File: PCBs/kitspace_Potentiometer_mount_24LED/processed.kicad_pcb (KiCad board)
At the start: 2 copper layers, 143.6 x 36.5 mm, 27 parts

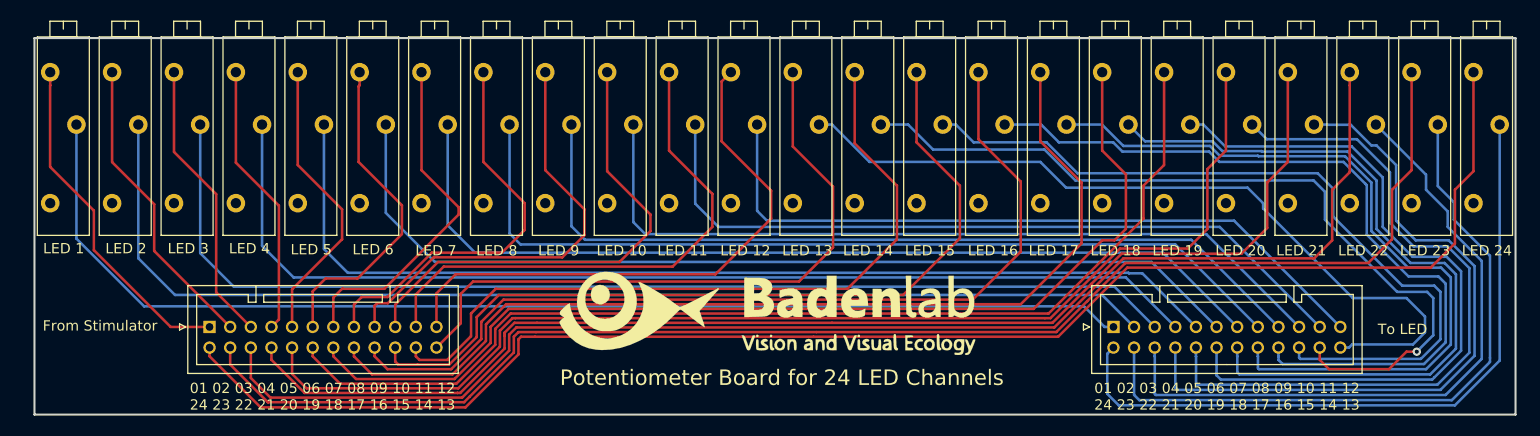
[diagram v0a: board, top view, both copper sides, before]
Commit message: recheck all circuits and clean up fill zone by rerouting the nets using freerouting and manually
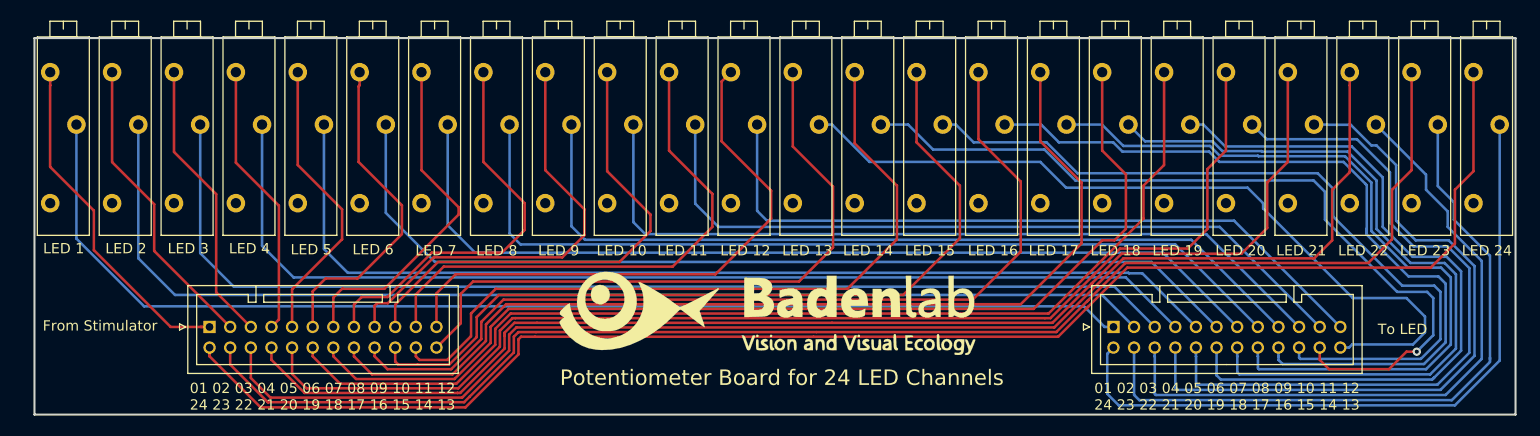
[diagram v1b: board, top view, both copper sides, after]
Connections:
-  LED 11 pad 1: (no net) -> Net-(RV11-Pad1)
- LED 1 pad 1: (no net) -> Net-(RV1-Pad1)
- LED 10 pad 1: (no net) -> Net-(RV10-Pad1)
- LED 12 pad 1: (no net) -> Net-(RV12-Pad1)
- LED 13 pad 1: (no net) -> Net-(RV13-Pad1)
- LED 14 pad 1: (no net) -> Net-(RV14-Pad1)
- LED 15 pad 1: (no net) -> Net-(RV15-Pad1)
- LED 16 pad 1: (no net) -> Net-(RV16-Pad1)
- LED 17 pad 1: (no net) -> Net-(RV17-Pad1)
- LED 18 pad 1: (no net) -> Net-(RV18-Pad1)
- LED 19 pad 1: (no net) -> Net-(RV19-Pad1)
- LED 2 pad 1: (no net) -> Net-(RV2-Pad1)
- LED 20 pad 1: (no net) -> Net-(RV20-Pad1)
- LED 21 pad 1: (no net) -> Net-(RV21-Pad1)
- LED 22 pad 1: (no net) -> Net-(RV22-Pad1)
- LED 23 pad 1: (no net) -> Net-(RV23-Pad1)
- LED 24 pad 1: (no net) -> Net-(RV24-Pad1)
- LED 3 pad 1: (no net) -> Net-(RV3-Pad1)
- LED 4 pad 1: (no net) -> Net-(RV4-Pad1)
- LED 5 pad 1: (no net) -> Net-(RV5-Pad1)
- LED 6 pad 1: (no net) -> Net-(RV6-Pad1)
- LED 7 pad 1: (no net) -> Net-(RV7-Pad1)
- LED 8 pad 1: (no net) -> Net-(RV8-Pad1)
- LED 9 pad 1: (no net) -> Net-(RV9-Pad1)
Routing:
- net Net-(J1-Pad24): track 148.4 -> 149.5 mm
- net Net-(J1-Pad1): track 33.3 -> 34.2 mm
- net Net-(J2-Pad16): track 76.1 -> 76.7 mm
